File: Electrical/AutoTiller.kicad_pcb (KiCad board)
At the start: 2 copper layers, 100 x 100 mm, 64 parts, among them J1 3220-14-0300-00, J2 USB_C_Receptacle_USB2.0, J3 T4145415031-001, SW1 DS04-254-2L-01BK, SW2 TS04-66-65-BK-160-SMT, SW3 TS04-66-65-BK-160-SMT, SW4 TS04-66-65-BK-160-SMT, SW5 TS04-66-65-BK-160-SMT, SW6 TS04-66-65-BK-160-SMT, SW7 TS04-66-65-BK-160-SMT, U1 STM32F103T6Ux, U2 TUSB320LAI, U3 IIS2MDCTR, U4 MAX22201, U6 VO615A-4, Y1 16 MHz

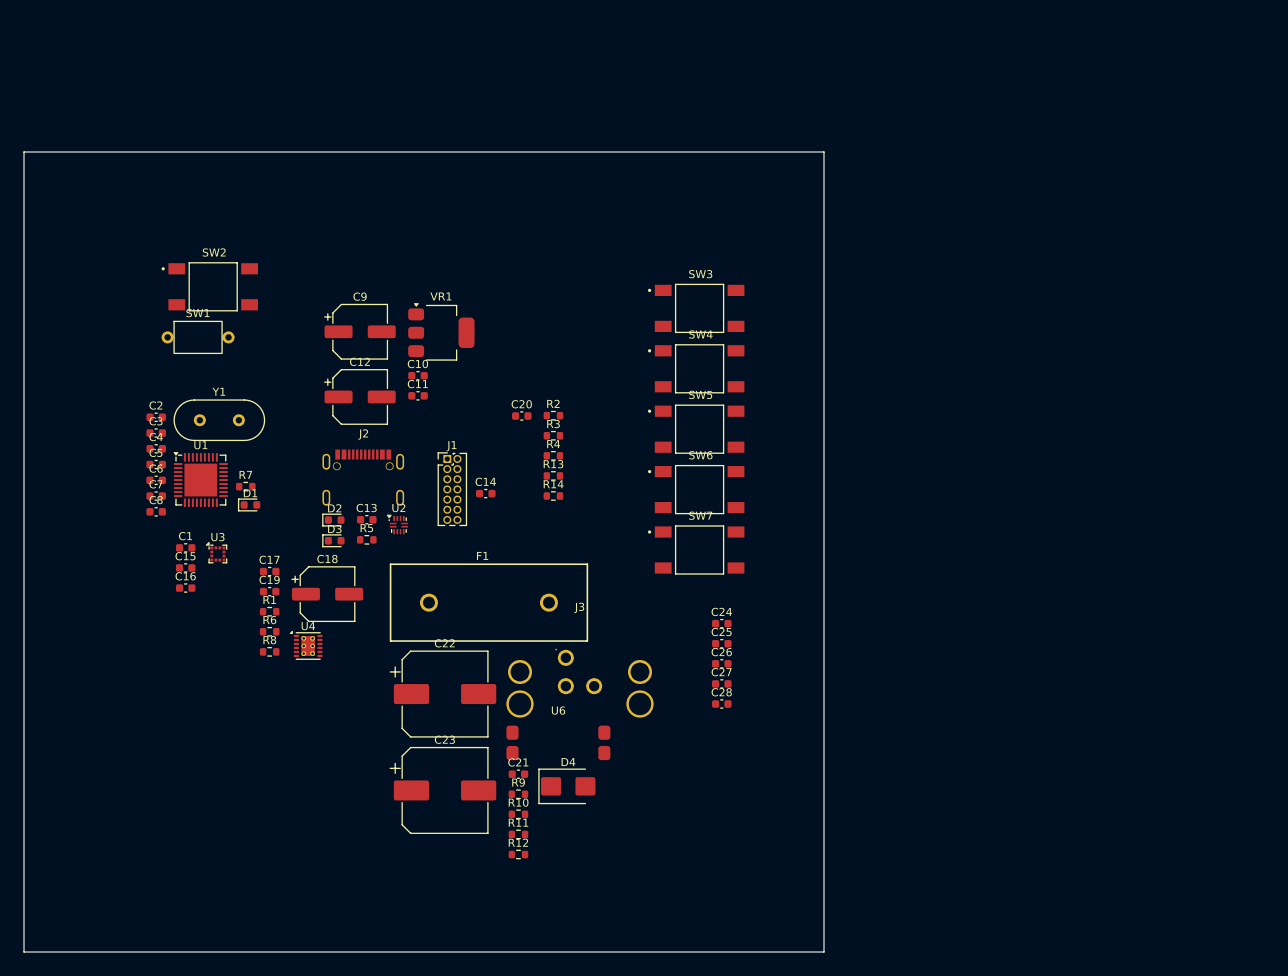
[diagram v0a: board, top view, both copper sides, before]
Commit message: Added layout for prototype 1
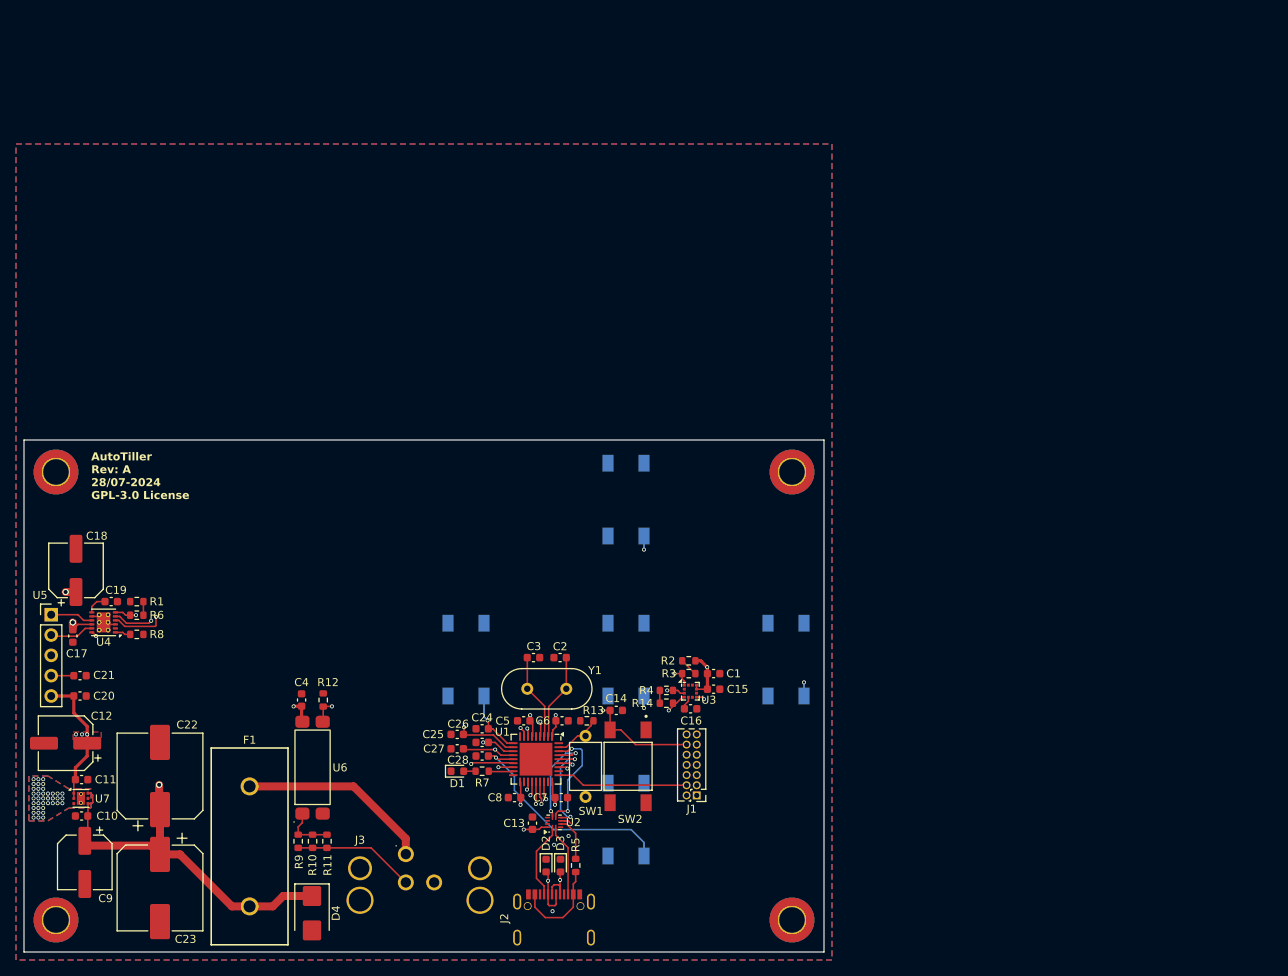
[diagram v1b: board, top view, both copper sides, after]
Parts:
- removed VR1: AP7361C-33E-13, Package_TO_SOT_SMD:SOT-223
- added H1: MountingHole, MountingHole:MountingHole_3.2mm_M3_DIN965_Pad_TopBottom, F.Cu at (115.0, 146.0)
- added H2: MountingHole, MountingHole:MountingHole_3.2mm_M3_DIN965_Pad_TopBottom, F.Cu at (207.0, 146.0)
- added H3: MountingHole, MountingHole:MountingHole_3.2mm_M3_DIN965_Pad_TopBottom, F.Cu at (207.0, 90.0)
- added H4: MountingHole, MountingHole:MountingHole_3.2mm_M3_DIN965_Pad_TopBottom, F.Cu at (115.0, 90.0)
- added U5: BHTGA-A-DW, Connector_PinHeader_2.54mm:PinHeader_1x05_P2.54mm_Vertical, F.Cu at (114.4, 107.8)
- added U7: TLV76733DRVx, Package_SON:WSON-6-1EP_2x2mm_P0.65mm_EP1x1.6mm_ThermalVias, F.Cu at (118.1, 130.8)
- SW3, SW4, SW5, SW6, SW7: moved to B.Cu
- moved SW2 79.6 mm to (186.8, 126.9), turned to -90 degrees
- moved C9 74.7 mm to (118.6, 138.8), turned to -90 degrees
- moved SW1 72.3 mm to (181.2, 126.8), turned to -90 degrees
- moved C10 69.3 mm to (118.2, 133.0), turned to 180 degrees
- moved C1 67.8 mm to (197.2, 115.2)
- moved C15 67.7 mm to (197.2, 117.2)
- moved C20 65.4 mm to (118.0, 118.0)
- moved C16 64.9 mm to (194.3, 119.6)
- moved SW3 64.6 mm to (186.5, 133.3), turned to 90 degrees
- moved C11 63.8 mm to (118.2, 128.4)
- moved C7 63.1 mm to (178.2, 130.7)
- moved U3 61.5 mm to (194.3, 117.4)
- moved J2 59.9 mm to (177.4, 148.2)
- moved C6 59.0 mm to (178.3, 121.1)
- moved C2 58.8 mm to (178.0, 113.2)
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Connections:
- net /USB_DM renamed /USB_D-
- net /USB_DP renamed /USB_D+
- SW3 pad 1: Net-(U1-PA3) -> Net-(U1-PA7)
- SW4 pad 1: Net-(U1-PA4) -> Net-(U1-PA5)
- SW5 pad 1: Net-(U1-PA5) -> Net-(U1-PA6)
- SW6 pad 1: Net-(U1-PA6) -> Net-(U1-PA3)
- SW7 pad 1: Net-(U1-PA7) -> Net-(U1-PA4)
- U4 pad 11: /Motor Driver/OUT_1 -> /Motor Driver/OUT_2
- U4 pad 9: /Motor Driver/OUT_2 -> /Motor Driver/OUT_1
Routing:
- net VDD: track 0.00 -> 81.8 mm, vias 0 -> 3
- net /Motor Driver/FAULT: track 0.00 -> 68.3 mm, vias 0 -> 2
- net /Processor/ACTUATOR_POT: track 0.00 -> 65.2 mm, vias 0 -> 1
- net /Motor Driver/IN1: track 0.00 -> 59.9 mm, vias 0 -> 2
- net /Motor Driver/ISEN: track 0.00 -> 57.9 mm, vias 0 -> 2
- net /Motor Driver/IN2: track 0.00 -> 57.9 mm, vias 0 -> 2
- net UART_RX: track 0.00 -> 57.1 mm, vias 0 -> 2
- net Net-(U1-PA6): track 0.00 -> 55.0 mm, vias 0 -> 2
- net Net-(U1-PA4): track 0.00 -> 52.1 mm, vias 0 -> 2
- net +3.3V: track 0.00 -> 43.3 mm, vias 0 -> 11
- net /E-Compass/I2C_SCL: track 0.00 -> 34.2 mm, vias 0 -> 3
- net /E-Compass/I2C_SDA: track 0.00 -> 30.4 mm, vias 0 -> 3
- net Net-(U1-PA7): track 0.00 -> 28.9 mm, vias 0 -> 1
- net Net-(U1-PA5): track 0.00 -> 27.6 mm, vias 0 -> 2
- net /Processor/UART_TX: track 0.00 -> 26.4 mm, vias 0 -> 1
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- added copper zone on F.Cu, net +3.3V
- added copper zone on In2.Cu, net +3.3V
- added copper zone on B.Cu, net GND
- added copper zone on F.Cu, net GND
- added copper zone on In1.Cu, net GND
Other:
- board size 100 x 100 mm -> 100 x 64 mm
- copper layers 2 -> 4
- board text added: "AutoTiller Rev: A 28/07-2024 GPL-3.0 License"
- board text added: "Motor"

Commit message: Finalizing the layout
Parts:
- removed C18, C9: 47uF, Capacitor_SMD:CP_Elec_6.3x7.7
- removed SW3: TS04-66-65-BK-160-SMT, AutoTiller:TS04-66-65-BK-160-SMT
- SW4, SW5, SW6, SW7: value TS04-66-65-BK-160-SMT -> TS04-66-95-BK-260-SMT
- moved C10 135.3 mm to (248.4, 96.2)
- moved C11 135.3 mm to (248.4, 91.7)
- moved C12 135.3 mm to (246.4, 87.1)
- moved U7 135.3 mm to (248.3, 94.0)
- moved U5 126.3 mm to (238.6, 84.6), turned to -90 degrees
- moved C17 121.1 mm to (235.9, 87.3), turned to 180 degrees
- moved C19 119.2 mm to (240.2, 92.1), turned to -90 degrees
- moved U4 118.0 mm to (237.6, 91.2), turned to 90 degrees
- moved C22 118.0 mm to (243.5, 104.0)
- moved J2 117.5 mm to (251.6, 57.2), turned to 90 degrees
- moved C21 116.2 mm to (231.0, 88.2), turned to -90 degrees
- moved R1 115.6 mm to (240.2, 95.3), turned to -90 degrees
- moved C20 114.4 mm to (228.4, 88.2), turned to -90 degrees
- moved R6 114.1 mm to (238.5, 95.3), turned to 90 degrees
- moved R8 112.0 mm to (236.1, 95.3), turned to 90 degrees
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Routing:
- net /Motor Driver/IN1: track 59.9 -> 7.82 mm, vias 2 -> 1
- net /Motor Driver/IN2: track 57.9 -> 6.48 mm, vias 2 -> 1
- net /Processor/ACTUATOR_POT: track 65.2 -> 15.9 mm
- net VDD: track 81.8 -> 33.1 mm, vias 3 -> 1
- net /Motor Driver/FAULT: track 68.3 -> 22.2 mm
- net /Motor Driver/ISEN: track 57.9 -> 17.5 mm
- net Net-(U1-PA7): track 28.9 -> 3.28 mm
- net Net-(U1-PA6): track 55.0 -> 30.3 mm, vias 2 -> 1
- net UART_RX: track 57.1 -> 34.5 mm
- net Net-(U1-PA4): track 52.1 -> 33.4 mm, vias 2 -> 1
- net /Processor/SWCLK: track 21.1 -> 7.39 mm
- net /Processor/SWDIO: track 16.5 -> 3.61 mm
- net /E-Compass/I2C_SCL: track 34.2 -> 22.3 mm
- net Net-(J3-Pin_2): track 15.2 -> 3.60 mm
- net /E-Compass/INT/DRDY: track 22.7 -> 11.2 mm
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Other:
- board size 100 x 64 mm -> 80.4 x 80.2 mm
